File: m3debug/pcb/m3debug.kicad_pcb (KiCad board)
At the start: 2 copper layers, 50 x 50 mm, 65 parts, among them IC1 STM32F405RxTx, IC2 MCP2562, IC3 ADP3335, J1 WEST TOP, J10 5V_SUPPLY, J11 CAN_SUPPLY, J12 3V3_SUPPLY, J13 PWRSW, J14 GND, J2 WEST BOT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

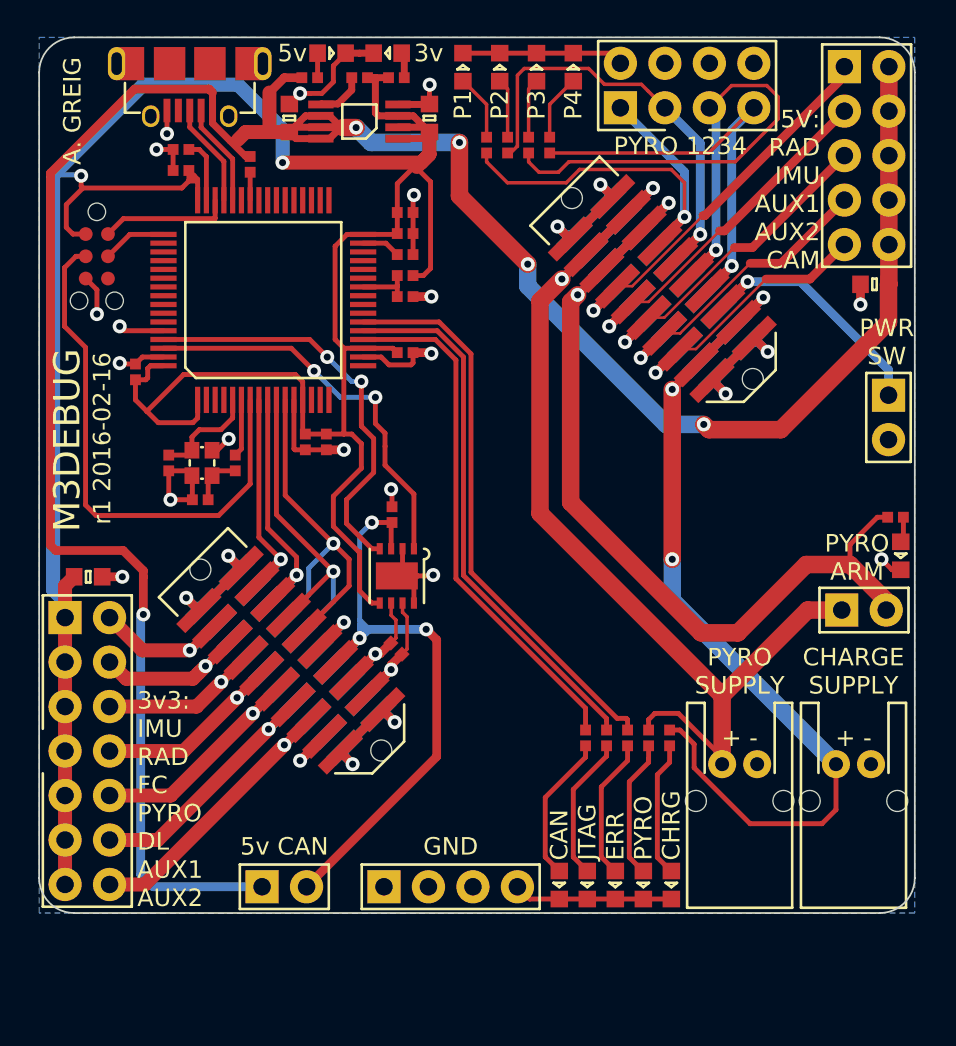
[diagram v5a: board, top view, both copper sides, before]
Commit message: Add routing for m3debug
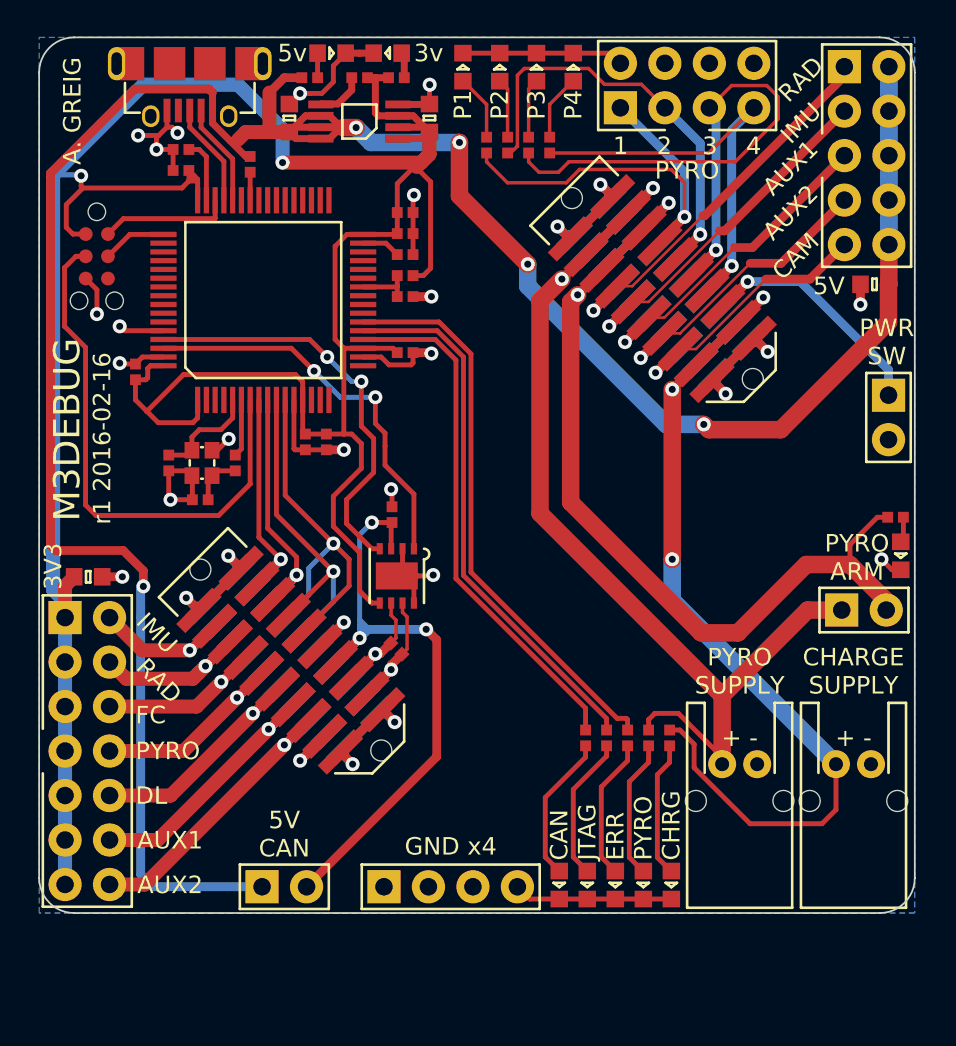
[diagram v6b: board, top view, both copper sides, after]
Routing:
- net GND: track 113.1 -> 116.1 mm, vias 26 -> 27
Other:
- board text added: "1"
- board text added: "2"
- board text added: "3"
- board text added: "3V3"
- board text added: "4"
- board text added: "5V"
- board text added: "5V CAN"
- board text added: "AUX1"
- board text added: "AUX2"
- board text added: "CAM"
- board text added: "DL"
- board text added: "FC"
- board text added: "GND x4"
- board text added: "IMU"
- board text added: "RAD"
- board text removed: "3v3: IMU RAD FC PYRO DL AUX1 AUX2"
- board text removed: "5V: RAD IMU AUX1 AUX2 CAM"
- board text removed: "5v CAN"
- board text removed: "GND"
- board text removed: "PYRO 1234"
